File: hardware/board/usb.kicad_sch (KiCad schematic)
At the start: 22 parts, among them J501 USB_B_Micro, J502 USB_C_Receptacle_PowerOnly_24P, P501 USB_C_Plug_USB2.0, U501 AP22653W6, U502 FSUSB42MX, U503 TPS259531DSGR

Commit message: finish swd, usb status, starting uart out and rp2350 remap?
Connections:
- net +5V: now also C501.1, C502.1, U501.1 (IN)
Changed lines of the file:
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@@
+	)
+	(junction
+		(at 69.85 53.34)
+		(diameter 0)
+		(color 0 0 0 0)
 	)
 	(junction
@@
 	)
 	(junction
+		(at 78.74 53.34)
+		(diameter 0)
+		(color 0 0 0 0)
+	)
+	(junction
 		(at 90.17 58.42)
 		(diameter 0)
@@
 		)
 		(stroke
+			(width 0)
+			(type default)
+		)
+	)
+	(wire
+		(pts
+			(xy 69.85 53.34) (xy 78.74 53.34)
+		)
+		(stroke

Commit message: fillout LCSC and swap micro usb
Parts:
- J501: footprint CM4IO:USB_Micro-B_EDAC_UCON00686 -> Connector_USB:USB_Micro-B_Molex_47346-0001; LCSC (none) -> C132560
- J502, P501: LCSC (none) -> C165948
- U501: LCSC (none) -> C2158037
- U502: value FSUSB42MX -> FSUSB42MUX; LCSC (none) -> C11355
- U503: Availability In Stock -> (none); LCSC (none) -> C2155674; Package WSON-8 Texas Instruments -> (none); Price None -> (none)
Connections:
- no-connect marks 0 -> 1
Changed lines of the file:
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@@
 		(color 0 0 0 0)
 	)
+	(no_connect
+		(at 88.9 114.3)
+	)
 	(wire
 		(pts
@@
 			)
 		)
+		(property "LCSC" "C165948"
+			(at 36.83 160.02 0)
+			(hide yes)
+			(show_name no)
+			(do_not_autoplace no)
+			(effects
+				(font
+					(size 1.27 1.27)
+				)
+			)
+		)
 		(pin "B4"
 		)
@@
 			)
 		)
+		(property "LCSC" "C2158037"
+			(at 105.41 55.88 0)
+			(hide yes)
+			(show_name no)
+			(do_not_autoplace no)
+			(effects
+				(font
+					(size 1.27 1.27)
+				)
+			)
+		)
 		(pin "1"
 		)
@@
 			)
 		)
-		(property "Package" "WSON-8 Texas Instruments"
-			(at 109.22 160.02 0)
-			(hide yes)
-			(show_name no)
-			(do_not_autoplace no)
-			(effects
-				(font
-					(size 1.27 1.27)
-				)
-				(justify bottom)
-			)
-		)
-		(property "Price" "None"
-			(at 109.22 160.02 0)
-			(hide yes)
-			(show_name no)
-			(do_not_autoplace no)
-			(effects
-				(font
-					(size 1.27 1.27)
-				)
-				(justify bottom)
-			)
-		)
 		(property "Check_prices" "https://www.snapeda.com/parts/TPS259531DSGR/Texas+Instruments/view-part/?ref=eda"
 			(at 109.22 160.02 0)
@@
 			)
 		)
-		(property "Availability" "In Stock"
+		(property "MANUFACTURER" "Texas Instruments"
 			(at 109.22 160.02 0)
 			(hide yes)
@@
 			)
 		)
-		(property "MANUFACTURER" "Texas Instruments"
+		(property "LCSC" "C2155674"
 			(at 109.22 160.02 0)
 			(hide yes)
@@
 					(size 1.27 1.27)
 				)
-				(justify bottom)
 			)
 		)
@@
 			)
 		)
-		(property "Footprint" "CM4IO:USB_Micro-B_EDAC_UCON00686"
+		(property "Footprint" "Connector_USB:USB_Micro-B_Molex_47346-0001"
 			(at 85.09 110.49 0)
 			(hide yes)
@@
 			)
 		)
+		(property "LCSC" "C132560"
+			(at 81.28 109.22 0)
+			(hide yes)
+			(show_name no)
+			(do_not_autoplace no)
+			(effects
+				(font
+					(size 1.27 1.27)
+				)
+			)
+		)
 		(pin "5"
 		)
@@
 			)
 		)
-		(property "Value" "FSUSB42MX"
+		(property "Value" "FSUSB42MUX"
 			(at 147.32 109.22 0)
 			(show_name no)
@@
 			)
 		)
+		(property "LCSC" "C11355"
+			(at 148.59 130.81 0)
+			(hide yes)
+			(show_name no)
+			(do_not_autoplace no)
+			(effects
+				(font
+					(size 1.27 1.27)
+				)
+			)
+		)
 		(pin "10"
 		)
@@
 			(at 204.47 68.58 0)
 			(hide yes)
+			(show_name no)
+			(do_not_autoplace no)
+			(effects
+				(font
+					(size 1.27 1.27)
+				)
+			)
+		)
+		(property "LCSC" "C165948"
+			(at 204.47 68.58 0)
+			(hide yes)

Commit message: finish LCSC
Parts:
- C501: LCSC (none) -> C1713
- C502, C503: value 0.1uF -> 100nF; LCSC (none) -> C49678
- C504: LCSC (none) -> C28323
- C505: LCSC (none) -> C1738
- R501, R503: LCSC (none) -> C17756
- R502: LCSC (none) -> C17719
- R504, R506: LCSC (none) -> C17414
- R505: LCSC (none) -> C17520
- R507: LCSC (none) -> C6351850
- R508: LCSC (none) -> C17656
- R509: LCSC (none) -> C17800
- R510, R511: LCSC (none) -> C26023
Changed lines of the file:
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@@
 			)
 		)
-		(property "Value" "0.1uF"
+		(property "Value" "100nF"
 			(at 81.28 144.7862 0)
 			(show_name no)
@@
 			)
 		)
+		(property "LCSC" "C49678"
+			(at 83.82 143.51 0)
+			(hide yes)
+			(show_name no)
+			(do_not_autoplace no)
+			(effects
+				(font
+					(size 1.27 1.27)
+				)
+			)
+		)
 		(pin "2"
 		)
@@
 			)
 		)
+		(property "LCSC" "C17756"
+			(at 184.15 58.42 90)
+			(hide yes)
+			(show_name no)
+			(do_not_autoplace no)
+			(effects
+				(font
+					(size 1.27 1.27)
+				)
+			)
+		)
 		(pin "2"
 		)
@@
 			)
 		)
+		(property "LCSC" "C17656"
+			(at 80.01 167.64 0)
+			(hide yes)
+			(show_name no)
+			(do_not_autoplace no)
+			(effects
+				(font
+					(size 1.27 1.27)
+				)
+			)
+		)
 		(pin "2"
 		)
@@
 			)
 		)
+		(property "LCSC" "C1738"
+			(at 91.44 165.1 0)
+			(hide yes)
+			(show_name no)
+			(do_not_autoplace no)
+			(effects
+				(font
+					(size 1.27 1.27)
+				)
+			)
+		)
 		(pin "2"
 		)
@@
 			)
 		)
+		(property "LCSC" "C17800"
+			(at 135.89 167.64 0)
+			(hide yes)
+			(show_name no)
+			(do_not_autoplace no)
+			(effects
+				(font
+					(size 1.27 1.27)
+				)
+			)
+		)
 		(pin "2"
 		)
@@
 			)
 		)
+		(property "LCSC" "C6351850"
+			(at 80.01 156.21 0)
+			(hide yes)
+			(show_name no)
+			(do_not_autoplace no)
+			(effects
+				(font
+					(size 1.27 1.27)
+				)
+			)
+		)
 		(pin "2"
 		)
@@
 			)
 		)
+		(property "LCSC" "C17756"
+			(at 184.15 60.96 90)
+			(hide yes)
+			(show_name no)
+			(do_not_autoplace no)
+			(effects
+				(font
+					(size 1.27 1.27)
+				)
+			)
+		)
 		(pin "2"
 		)
@@
 			)
 		)
+		(property "LCSC" "C17414"
+			(at 128.27 146.05 0)
+			(hide yes)
+			(show_name no)
+			(do_not_autoplace no)
+			(effects
+				(font
+					(size 1.27 1.27)
+				)
+			)
+		)
 		(pin "2"
 		)
@@
 			)
 		)
+		(property "LCSC" "C17414"
+			(at 69.85 67.31 0)
+			(hide yes)
+			(show_name no)
+			(do_not_autoplace no)
+			(effects
+				(font
+					(size 1.27 1.27)
+				)
+			)
+		)
 		(pin "2"
 		)
@@
 			)
 		)
-		(property "Value" "0.1uF"
+		(property "Value" "100nF"
 			(at 87.63 57.1562 0)
 			(show_name no)
@@
 			)
 		)
+		(property "LCSC" "C49678"
+			(at 90.17 55.88 0)
+			(hide yes)
+			(show_name no)
+			(do_not_autoplace no)
+			(effects
+				(font
+					(size 1.27 1.27)
+				)
+			)
+		)
 		(pin "1"
 		)
@@
 			)
 		)
+		(property "LCSC" "C1713"
+			(at 78.74 55.88 0)
+			(hide yes)
+			(show_name no)
+			(do_not_autoplace no)
+			(effects
+				(font
+					(size 1.27 1.27)
+				)
+			)
+		)
 		(pin "1"
 		)
@@
 			)
 		)
+		(property "LCSC" "C26023"
+			(at 63.5 173.99 0)
+			(hide yes)
+			(show_name no)
+			(do_not_autoplace no)
+			(effects
+				(font
+					(size 1.27 1.27)
+				)
+			)
+		)
 		(pin "2"
 		)
@@
 			)
 		)
+		(property "LCSC" "C17520"
+			(at 167.64 110.49 0)
+			(hide yes)
+			(show_name no)
+			(do_not_autoplace no)
+			(effects
+				(font
+					(size 1.27 1.27)
+				)
+			)
+		)
 		(pin "1"
 		)
@@
 			)
 		)
+		(property "LCSC" "C17719"
+			(at 120.65 60.96 0)
+			(hide yes)
+			(show_name no)
+			(do_not_autoplace no)
+			(effects
+				(font
+					(size 1.27 1.27)
+				)
+			)
+		)
 		(pin "2"
 		)
@@
 			)
 		)
+		(property "LCSC" "C26023"
+			(at 60.96 173.99 0)
+			(hide yes)
+			(show_name no)
+			(do_not_autoplace no)
+			(effects
+				(font
+					(size 1.27 1.27)
+				)
+			)
+		)
 		(pin "2"
 		)
@@
 			(at 151.13 154.94 0)
 			(hide yes)
+			(show_name no)
+			(do_not_autoplace no)
+			(effects
+				(font
+					(size 1.27 1.27)
+				)
+			)
+		)
+		(property "LCSC" "C28323"
+			(at 151.13 154.94 0)
+			(hide yes)

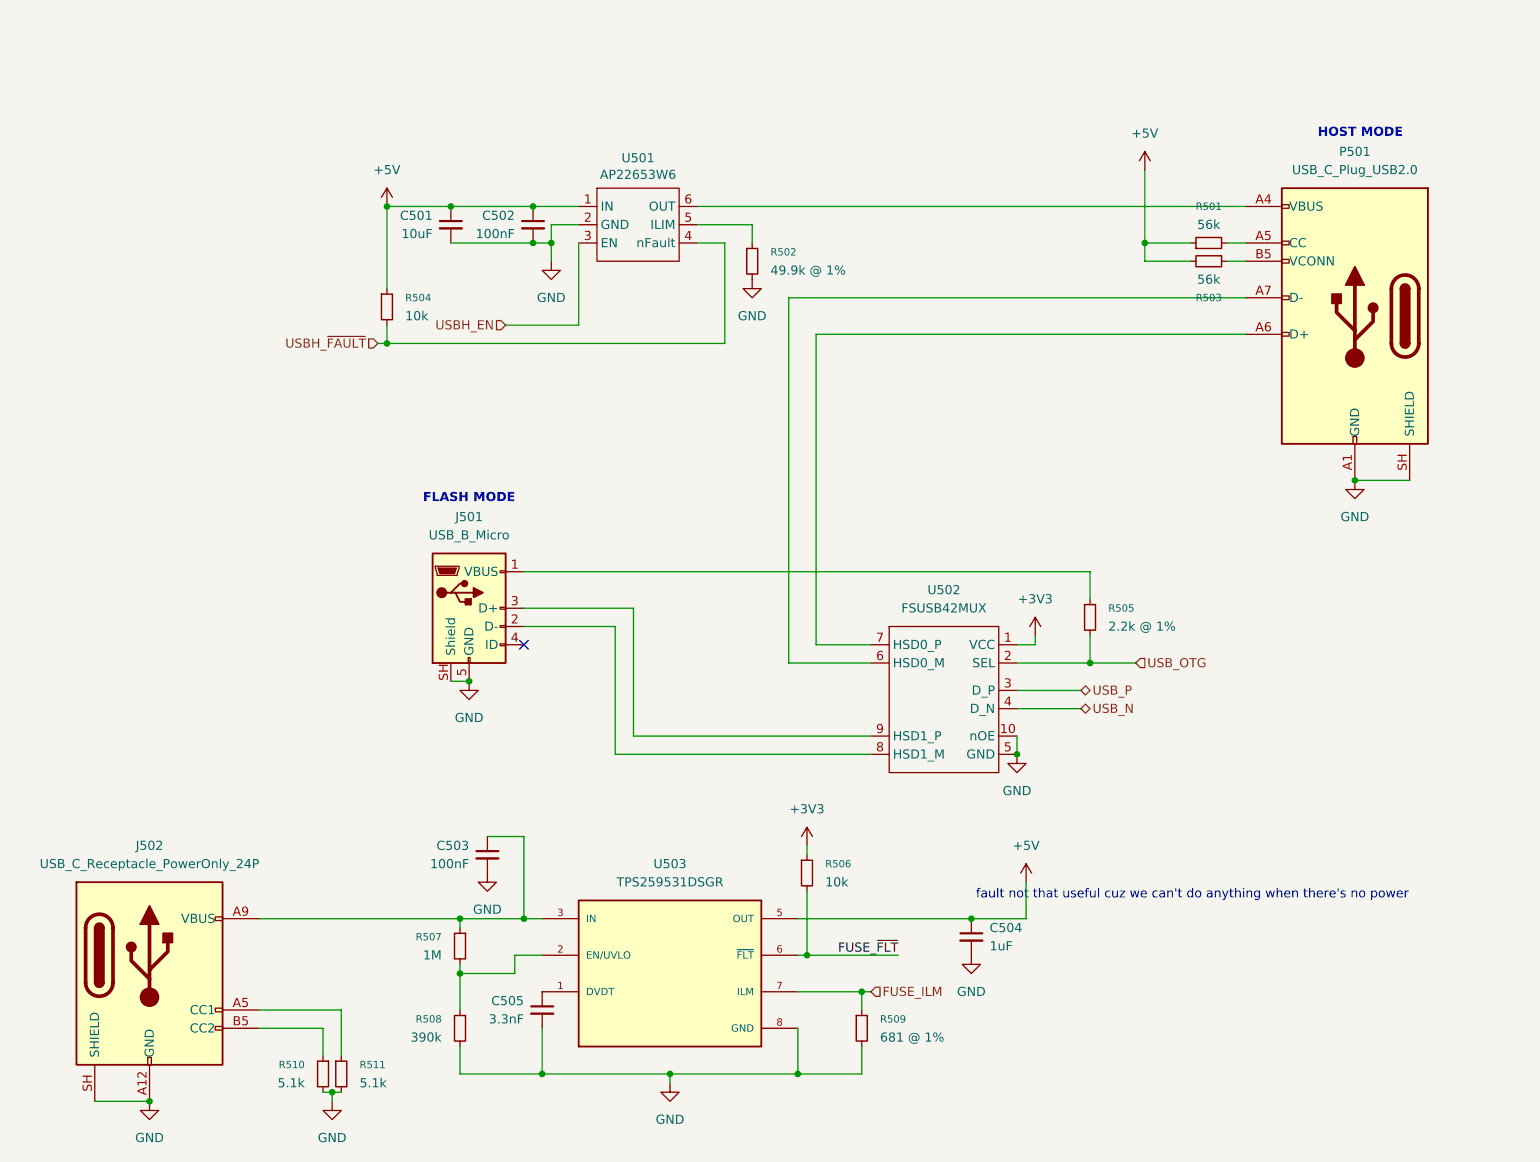
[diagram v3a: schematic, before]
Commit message: 3v3out, delete usb, add leds, LDO
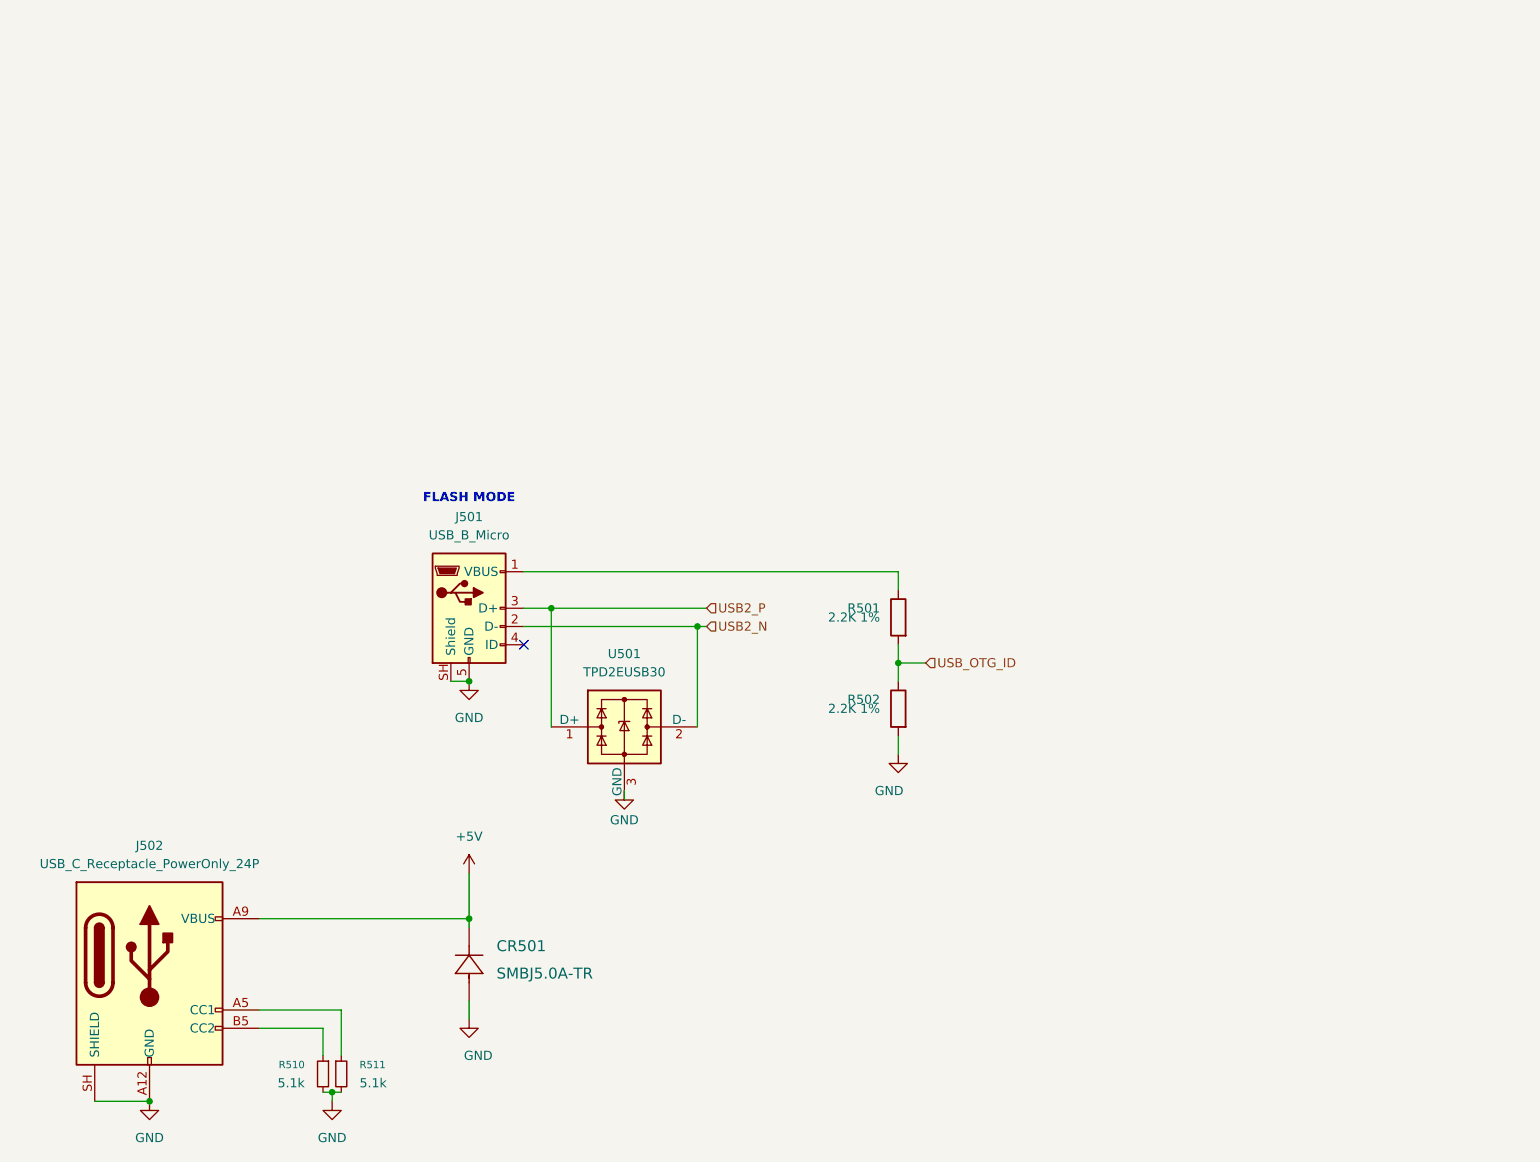
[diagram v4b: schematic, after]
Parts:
- removed C501: 10uF, Capacitor_SMD:C_0805_2012Metric, symbol Device:C_Small
- removed C502, C503: 100nF, Capacitor_SMD:C_0805_2012Metric, symbol Device:C_Small
- removed C504: 1uF, Capacitor_SMD:C_0805_2012Metric, symbol Device:C_Small
- removed C505: 3.3nF, Capacitor_SMD:C_0805_2012Metric, symbol Device:C_Small
- removed P501: USB_C_Plug_USB2.0, Connector_USB:USB_C_Receptacle_HRO_TYPE-C-31-M-12, symbol Connector:USB_C_Plug_USB2.0
- removed R501, R503: 56k, Resistor_SMD:R_0805_2012Metric, symbol Device:R_Small
- removed R502: 49.9k @ 1%, Resistor_SMD:R_0805_2012Metric, symbol Device:R_Small
- removed R504, R506: 10k, Resistor_SMD:R_0805_2012Metric, symbol Device:R_Small
- removed R505: 2.2k @ 1%, Resistor_SMD:R_0805_2012Metric, symbol Device:R_Small
- removed R507: 1M, Resistor_SMD:R_0805_2012Metric, symbol Device:R_Small
- removed R508: 390k, Resistor_SMD:R_0805_2012Metric, symbol Device:R_Small
- removed R509: 681 @ 1%, Resistor_SMD:R_0805_2012Metric, symbol Device:R_Small
- removed U501: AP22653W6, Package_TO_SOT_SMD:SOT-23-6, symbol CM4IO:AP2553W6
- removed U502: FSUSB42MUX, Package_SO:MSOP-10_3x3mm_P0.5mm, symbol CM4IO:FSUSB42MX
- removed U503: TPS259531DSGR, ledaw:SON50P200X200X80-9N, symbol TPS259531DSGR:TPS259531DSGR
- added CR501: SMBJ5.0A-TR, footprints:SMBJ5.0A-TR, symbol 2020-11-06_22-01-36:SMBJ5.0A-TR
- added R501, R502: 2.2K 1%, Resistor_SMD:R_0603_1608Metric_Pad0.98x0.95mm_HandSolder, symbol Device:R
- added U501: TPD2EUSB30, Package_TO_SOT_SMD:Texas_DRT-3, symbol Power_Protection:TPD2EUSB30
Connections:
- net +5V: now also J502.A4 (VBUS), J502.A9 (VBUS), J502.B4 (VBUS), J502.B9 (VBUS), CR501.1
- net GND: now also CR501.2, R502.2, U501.3 (GND)
- net at J501.1 (VBUS): now also R501.1
- net USB2_N: now reaches J501.2 (D-)
- net USB2_N: now also U501.2 (D-)
- net USB2_P: now reaches J501.3 (D+)
- net USB2_P: now also U501.1 (D+)
- new net USB_OTG_ID: R501.2, R502.1
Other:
- note removed: "HOST MODE"
- note removed: "fault not that useful cuz we can't do anything when there's no power"

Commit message: giga test points
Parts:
- added TP501: VBUS, symbol Connector:TestPoint
- added TP502: USB_OTG_ID, symbol Connector:TestPoint
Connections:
- net +5V: now also TP501.1
- net USB_OTG_ID: now also TP502.1
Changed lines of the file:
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@@
+	)
+	(junction
+		(at 149.86 116.84)
+		(diameter 0)
+		(color 0 0 0 0)
+	)
+	(junction
+		(at 140.97 116.84)
+		(diameter 0)
+		(color 0 0 0 0)
 	)
 	(junction
@@
 	)
 	(junction
-		(at 140.97 116.84)
-		(diameter 0)
-		(color 0 0 0 0)
-	)
-	(junction
 		(at 81.28 152.4)
 		(diameter 0)
@@
 	)
 	(junction
+		(at 57.15 152.4)
+		(diameter 0)
+		(color 0 0 0 0)
+	)
+	(junction
 		(at 81.28 119.38)
 		(diameter 0)
@@
 	(wire
 		(pts
+			(xy 57.15 152.4) (xy 81.28 152.4)
+		)
+		(stroke
+			(width 0)
+			(type default)
+		)
+	)
+	(wire
+		(pts
 			(xy 62.23 176.53) (xy 63.5 176.53)
 		)
@@
 	(wire
 		(pts
-			(xy 144.78 116.84) (xy 140.97 116.84)
+			(xy 156.21 116.84) (xy 149.86 116.84)
 		)
 		(stroke
@@
 	(wire
 		(pts
-			(xy 140.97 104.14) (xy 88.9 104.14)
+			(xy 149.86 116.84) (xy 140.97 116.84)
 		)
 		(stroke
@@
 	(wire
 		(pts
+			(xy 88.9 104.14) (xy 140.97 104.14)
+		)
+		(stroke
+			(width 0)
+			(type solid)
+		)
+	)
+	(wire
+		(pts
 			(xy 102.87 135.89) (xy 102.87 134.62)
 		)
@@
 	(wire
 		(pts
-			(xy 52.07 152.4) (xy 81.28 152.4)
+			(xy 52.07 152.4) (xy 57.15 152.4)
 		)
 		(stroke
@@
 	(hierarchical_label "USB_OTG_ID"
 		(shape input)
-		(at 144.78 116.84 0)
+		(at 156.21 116.84 0)
 		(effects
 			(font
@@
 	)
 	(symbol
+		(lib_id "Connector:TestPoint")
+		(at 149.86 116.84 0)
+		(unit 1)
+		(body_style 1)
+		(exclude_from_sim no)
+		(in_bom yes)
+		(on_board yes)
+		(in_pos_files yes)
+		(dnp no)
+		(fields_autoplaced yes)
+		(property "Reference" "TP502"
+			(at 152.4 112.2679 0)
+			(show_name no)
+			(do_not_autoplace no)
+			(effects
+				(font
+					(size 1.27 1.27)
+				)
+				(justify left)
+			)
+		)
+		(property "Value" "USB_OTG_ID"
+			(at 152.4 114.8079 0)
+			(show_name no)
+			(do_not_autoplace no)
+			(effects
+				(font
+					(size 1.27 1.27)
+				)
+				(justify left)
+			)
+		)
+		(property "Footprint" ""
+			(at 154.94 116.84 0)
+			(hide yes)
+			(show_name no)
+			(do_not_autoplace no)
+			(effects
+				(font
+					(size 1.27 1.27)
+				)
+			)
+		)
+		(property "Datasheet" ""
+			(at 154.94 116.84 0)
+			(hide yes)
+			(show_name no)
+			(do_not_autoplace no)
+			(effects
+				(font
+					(size 1.27 1.27)
+				)
+			)
+		)
+		(property "Description" "test point"
+			(at 149.86 116.84 0)
+			(hide yes)
+			(show_name no)
+			(do_not_autoplace no)
+			(effects
+				(font
+					(size 1.27 1.27)
+				)
+			)
+		)
+		(pin "1"
+		)
+		(instances
+			(project "board"
+				(path "/dd13fd41-39ab-4435-9074-5024f1786746/e77fa723-60b4-4aaf-b8c0-33f73a50a054"
+					(reference "TP502")
+					(unit 1)
+				)
+			)
+		)
+	)
+	(symbol
 		(lib_id "power:+5V")
 		(at 81.28 146.05 0)
@@
 					(unit 1)
 				)
+			)
+		)
+	)
+	(symbol
+		(lib_id "Connector:TestPoint")
+		(at 57.15 152.4 0)
+		(unit 1)
+		(body_style 1)
+		(exclude_from_sim no)
+		(in_bom yes)
+		(on_board yes)
+		(in_pos_files yes)
+		(dnp no)
+		(fields_autoplaced yes)
+		(property "Reference" "TP501"
+			(at 59.69 147.8279 0)
+			(show_name no)
+			(do_not_autoplace no)
+			(effects
+				(font
+					(size 1.27 1.27)
+				)
+				(justify left)
+			)
+		)
+		(property "Value" "VBUS"
+			(at 59.69 150.3679 0)
+			(show_name no)
+			(do_not_autoplace no)
+			(effects
+				(font
+					(size 1.27 1.27)
+				)
+				(justify left)
+			)
+		)
+		(property "Footprint" ""
+			(at 62.23 152.4 0)
+			(hide yes)
+			(show_name no)
+			(do_not_autoplace no)
+			(effects
+				(font
+					(size 1.27 1.27)
+				)
+			)
+		)
+		(property "Datasheet" ""
+			(at 62.23 152.4 0)
+			(hide yes)
+			(show_name no)
+			(do_not_autoplace no)
+			(effects
+				(font
+					(size 1.27 1.27)
+				)
+			)
+		)
+		(property "Description" "test point"
+			(at 57.15 152.4 0)
+			(hide yes)
+			(show_name no)
+			(do_not_autoplace no)
+			(effects
+				(font
+					(size 1.27 1.27)
+				)
+			)
+		)
+		(pin "1"
+		)
+		(instances
+			(project "board"
+				(path "/dd13fd41-39ab-4435-9074-5024f1786746/e77fa723-60b4-4aaf-b8c0-33f73a50a054"
+					(reference "TP501")
+					(unit 1)
+				)

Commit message: footprints
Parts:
- CR501: footprint footprints:SMBJ5.0A-TR -> Diode_SMD:D_SMB
- R501, R502: footprint Resistor_SMD:R_0603_1608Metric_Pad0.98x0.95mm_HandSolder -> Resistor_SMD:R_0805_2012Metric
- TP501, TP502: footprint (none) -> TestPoint:TestPoint_Keystone_5015_Micro_Mini
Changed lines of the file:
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@@
 			)
 		)
-		(property "Footprint" "Resistor_SMD:R_0603_1608Metric_Pad0.98x0.95mm_HandSolder"
+		(property "Footprint" "Resistor_SMD:R_0805_2012Metric"
 			(at 142.748 123.19 90)
 			(hide yes)
@@
 			)
 		)
-		(property "Footprint" "footprints:SMBJ5.0A-TR"
+		(property "Footprint" "Diode_SMD:D_SMB"
 			(at 90.424 158.75 0)
 			(hide yes)
@@
 			)
 		)
-		(property "Footprint" ""
+		(property "Footprint" "TestPoint:TestPoint_Keystone_5015_Micro_Mini"
 			(at 154.94 116.84 0)
 			(hide yes)
@@
 			)
 		)
-		(property "Footprint" "Resistor_SMD:R_0603_1608Metric_Pad0.98x0.95mm_HandSolder"
+		(property "Footprint" "Resistor_SMD:R_0805_2012Metric"
 			(at 142.748 110.49 90)
 			(hide yes)
@@
 			)
 		)
-		(property "Footprint" ""
+		(property "Footprint" "TestPoint:TestPoint_Keystone_5015_Micro_Mini"
 			(at 62.23 152.4 0)
 			(hide yes)
